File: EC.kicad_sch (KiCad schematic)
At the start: 8 parts, among them CN2 B4B-ZR (LF)(SN), CN3 ZH1.5-6P-LT, CN4 B4B-ZR (LF)(SN), J1 Conn_01x06_Socket, J3 Conn_01x06_Socket, J5 Conn_01x10_Socket, J6 Conn_01x10_Socket

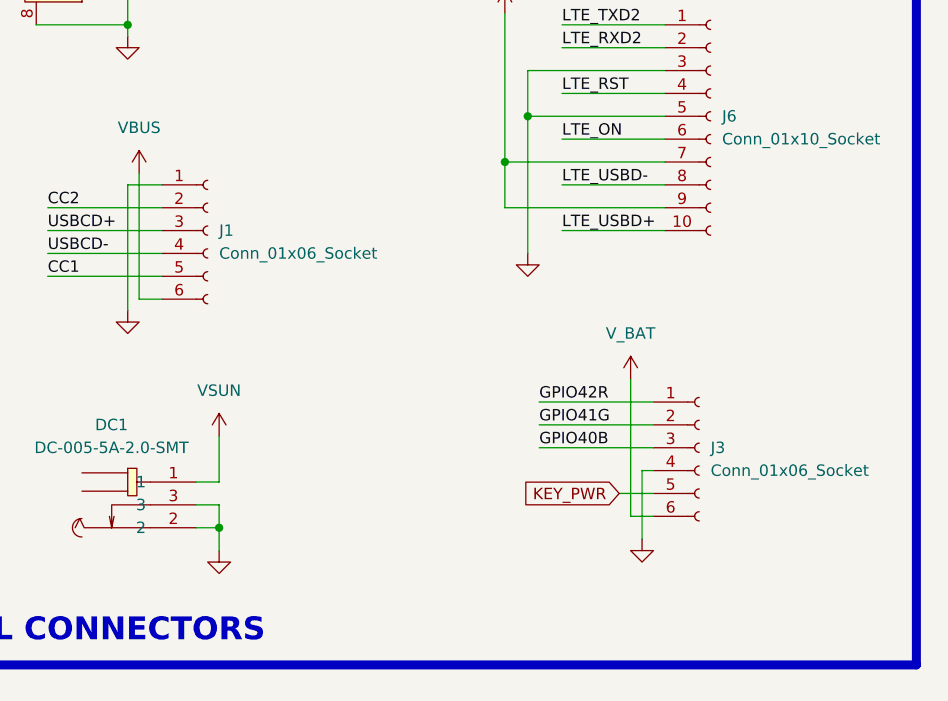
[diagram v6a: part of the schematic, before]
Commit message: [Schematic/PCB][Added] Routing finished, DRC finished
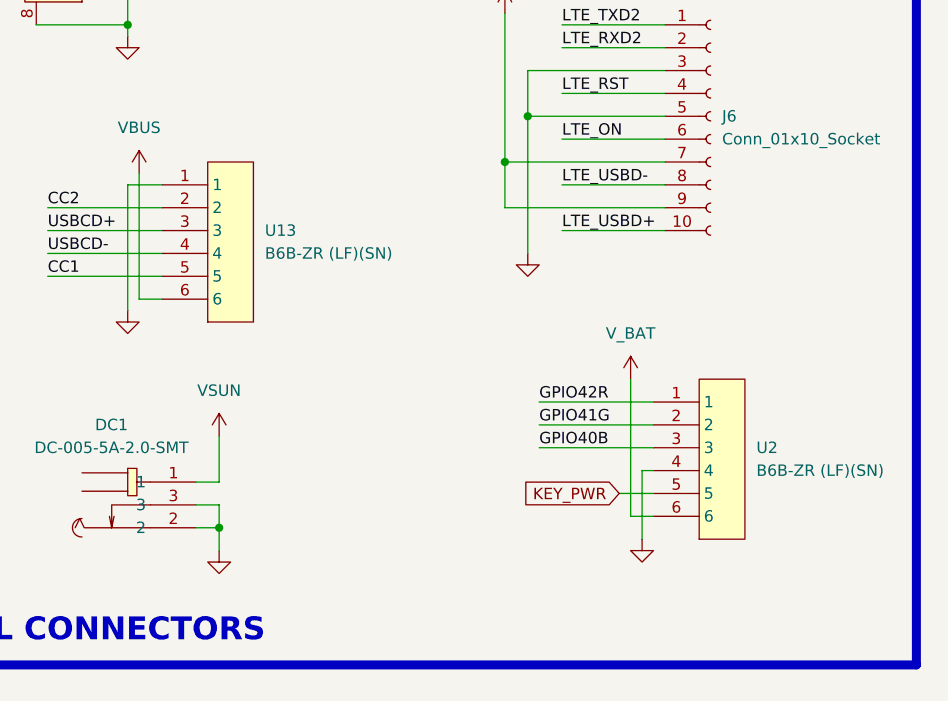
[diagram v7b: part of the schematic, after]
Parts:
- removed J1, J3: Conn_01x06_Socket, Connector_JST:JST_ZH_B6B-ZR_1x06_P1.50mm_Vertical, symbol Connector:Conn_01x06_Socket
- added U13, U2: B6B-ZR (LF)(SN), easyeda2kicad:CONN-TH-6P-P1.50_B6B-ZR-LF-SN, symbol easyeda2kicad:B6B-ZR(LF)(SN)
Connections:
- net CC1: now also U13.5
- net CC2: now also U13.2
- net GND: now also U13.1, U2.4
- net GPIO40B: now also U2.3
- net GPIO41G: now also U2.2
- net GPIO42R: now also U2.1
- net KEY_PWR: now also U2.5
- net USBCD+: now also U13.3
- net USBCD-: now also U13.4
- net VBUS: now also U13.6
- net V_BAT: now also U2.6
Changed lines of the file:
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@@
 	)
 	(symbol
-		(lib_id "Connector:Conn_01x06_Socket")
-		(at 224.79 125.73 0)
-		(unit 1)
-		(exclude_from_sim no)
-		(in_bom yes)
-		(on_board yes)
-		(dnp no)
-		(fields_autoplaced yes)
-		(property "Reference" "J3"
-			(at 226.06 125.7299 0)
-			(effects
-				(font
-					(size 1.27 1.27)
-				)
-				(justify left)
-			)
-		)
-		(property "Value" "Conn_01x06_Socket"
-			(at 226.06 128.2699 0)
-			(effects
-				(font
-					(size 1.27 1.27)
-				)
-				(justify left)
-			)
-		)
-		(property "Footprint" "Connector_JST:JST_ZH_B6B-ZR_1x06_P1.50mm_Vertical"
-			(at 224.79 125.73 0)
-			(effects
-				(font
-					(size 1.27 1.27)
-				)
-				(hide yes)
-			)
-		)
-		(property "Datasheet" "~"
-			(at 224.79 125.73 0)
-			(effects
-				(font
-					(size 1.27 1.27)
-				)
-				(hide yes)
-			)
-		)
-		(property "Description" "Generic connector, single row, 01x06, script generated"
-			(at 224.79 125.73 0)
-			(effects
-				(font
-					(size 1.27 1.27)
-				)
-				(hide yes)
-			)
+		(lib_id "easyeda2kicad:B6B-ZR(LF)(SN)")
+		(at 224.79 128.27 90)
+		(unit 1)
+		(exclude_from_sim no)
+		(in_bom yes)
+		(on_board yes)
+		(dnp no)
+		(fields_autoplaced yes)
+		(property "Reference" "U2"
+			(at 231.14 125.7299 90)
+			(effects
+				(font
+					(size 1.27 1.27)
+				)
+				(justify right)
+			)
+		)
+		(property "Value" "B6B-ZR (LF)(SN)"
+			(at 231.14 128.2699 90)
+			(effects
+				(font
+					(size 1.27 1.27)
+				)
+				(justify right)
+			)
+		)
+		(property "Footprint" "easyeda2kicad:CONN-TH-6P-P1.50_B6B-ZR-LF-SN"
+			(at 227.33 128.27 0)
+			(effects
+				(font
+					(size 1.27 1.27)
+				)
+				(hide yes)
+			)
+		)
+		(property "Datasheet" "https://lcsc.com/product-detail/_JST-Sales-America__JST-Sales-America-ZHseries-socket-1-6P-pitch1-5mm_C157984.html"
+			(at 229.87 128.27 0)
+			(effects
+				(font
+					(size 1.27 1.27)
+				)
+				(hide yes)
+			)
+		)
+		(property "Description" ""
+			(at 224.79 128.27 0)
+			(effects
+				(font
+					(size 1.27 1.27)
+				)
+				(hide yes)
+			)
+		)
+		(property "LCSC Part" "C157984"
+			(at 232.41 128.27 0)
+			(effects
+				(font
+					(size 1.27 1.27)
+				)
+				(hide yes)
+			)
+		)
+		(pin "3"
+		)
+		(pin "6"
+		)
+		(pin "5"
+		)
+		(pin "4"
 		)
 		(pin "2"
 		)
-		(pin "5"
-		)
-		(pin "3"
-		)
-		(pin "1"
-		)
-		(pin "4"
-		)
-		(pin "6"
-		)
-		(instances
-			(project "IndustrialSense"
-				(path "/f9e05184-c88b-4a88-ae9c-ab2bdb32be7c/c5103ceb-5325-4a84-a025-9638a412984e/5ac2d668-0304-4bbe-8771-56c1c044638f"
-					(reference "J3")
+		(pin "1"
+		)
+		(instances
+			(project ""
+				(path "/f9e05184-c88b-4a88-ae9c-ab2bdb32be7c/c5103ceb-5325-4a84-a025-9638a412984e/5ac2d668-0304-4bbe-8771-56c1c044638f"
+					(reference "U2")
 					(unit 1)
 				)
@@
 	)
 	(symbol
+		(lib_id "easyeda2kicad:B6B-ZR(LF)(SN)")
+		(at 170.18 104.14 90)
+		(unit 1)
+		(exclude_from_sim no)
+		(in_bom yes)
+		(on_board yes)
+		(dnp no)
+		(fields_autoplaced yes)
+		(property "Reference" "U13"
+			(at 176.53 101.5999 90)
+			(effects
+				(font
+					(size 1.27 1.27)
+				)
+				(justify right)
+			)
+		)
+		(property "Value" "B6B-ZR (LF)(SN)"
+			(at 176.53 104.1399 90)
+			(effects
+				(font
+					(size 1.27 1.27)
+				)
+				(justify right)
+			)
+		)
+		(property "Footprint" "easyeda2kicad:CONN-TH-6P-P1.50_B6B-ZR-LF-SN"
+			(at 172.72 104.14 0)
+			(effects
+				(font
+					(size 1.27 1.27)
+				)
+				(hide yes)
+			)
+		)
+		(property "Datasheet" "https://lcsc.com/product-detail/_JST-Sales-America__JST-Sales-America-ZHseries-socket-1-6P-pitch1-5mm_C157984.html"
+			(at 175.26 104.14 0)
+			(effects
+				(font
+					(size 1.27 1.27)
+				)
+				(hide yes)
+			)
+		)
+		(property "Description" ""
+			(at 170.18 104.14 0)
+			(effects
+				(font
+					(size 1.27 1.27)
+				)
+				(hide yes)
+			)
+		)
+		(property "LCSC Part" "C157984"
+			(at 177.8 104.14 0)
+			(effects
+				(font
+					(size 1.27 1.27)
+				)
+				(hide yes)
+			)
+		)
+		(pin "3"
+		)
+		(pin "6"
+		)
+		(pin "5"
+		)
+		(pin "4"
+		)
+		(pin "2"
+		)
+		(pin "1"
+		)
+		(instances
+			(project "IndustrialSense"
+				(path "/f9e05184-c88b-4a88-ae9c-ab2bdb32be7c/c5103ceb-5325-4a84-a025-9638a412984e/5ac2d668-0304-4bbe-8771-56c1c044638f"
+					(reference "U13")
+					(unit 1)
+				)
+			)
+		)
+	)
+	(symbol
 		(lib_id "power:VBUS")
 		(at 162.56 95.25 0)
@@
 					(unit 1)
 				)
-			)
-		)
-	)
-	(symbol
-		(lib_id "Connector:Conn_01x06_Socket")
-		(at 170.18 101.6 0)
-		(unit 1)
-		(exclude_from_sim no)
-		(in_bom yes)
-		(on_board yes)
-		(dnp no)
-		(fields_autoplaced yes)
-		(property "Reference" "J1"
-			(at 171.45 101.5999 0)
-			(effects
-				(font
-					(size 1.27 1.27)
-				)
-				(justify left)
-			)
-		)
-		(property "Value" "Conn_01x06_Socket"
-			(at 171.45 104.1399 0)
-			(effects
-				(font
-					(size 1.27 1.27)
-				)
-				(justify left)
-			)
-		)
-		(property "Footprint" "Connector_JST:JST_ZH_B6B-ZR_1x06_P1.50mm_Vertical"
-			(at 170.18 101.6 0)
-			(effects
-				(font
-					(size 1.27 1.27)
-				)
-				(hide yes)
-			)
-		)
-		(property "Datasheet" "~"
-			(at 170.18 101.6 0)
-			(effects
-				(font
-					(size 1.27 1.27)
-				)
-				(hide yes)
-			)
-		)
-		(property "Description" "Generic connector, single row, 01x06, script generated"
-			(at 170.18 101.6 0)
-			(effects
-				(font
-					(size 1.27 1.27)
-				)
-				(hide yes)
-			)
-		)
-		(pin "2"
-		)
-		(pin "5"
-		)
-		(pin "3"
-		)
-		(pin "1"
-		)
-		(pin "4"
-		)
-		(pin "6"
-		)
-		(instances
-			(project ""
-				(path "/f9e05184-c88b-4a88-ae9c-ab2bdb32be7c/c5103ceb-5325-4a84-a025-9638a412984e/5ac2d668-0304-4bbe-8771-56c1c044638f"
-					(reference "J1")
-					(unit 1)
-				)
